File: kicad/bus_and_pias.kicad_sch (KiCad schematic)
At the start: 5 parts, among them J1 Conn_02x17_Odd_Even, U1 MC68A21, U14 74LS02, U15 74LS138, U2 MC68A21

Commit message: KiCAD: Initial PCB placement
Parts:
- J1: footprint (none) -> Connector_PinHeader_2.54mm:PinHeader_2x17_P2.54mm_Vertical
- U1, U2: footprint Package_DIP:DIP-40_W15.24mm -> Package_DIP:DIP-40_W15.24mm_LongPads
- U14: footprint (none) -> Package_DIP:DIP-14_W7.62mm_LongPads
- U15: footprint (none) -> Package_DIP:DIP-16_W7.62mm_LongPads
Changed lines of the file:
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@@
       (effects (font (size 1.27 1.27)) (justify left))
     )
-    (property "Footprint" "Package_DIP:DIP-40_W15.24mm" (id 2) (at 238.76 129.54 0)
+    (property "Footprint" "Package_DIP:DIP-40_W15.24mm_LongPads" (id 2) (at 238.76 129.54 0)
       (effects (font (size 1.27 1.27)) (justify left) hide)
     )
@@
       (effects (font (size 1.27 1.27)) (justify left))
     )
-    (property "Footprint" "Package_DIP:DIP-40_W15.24mm" (id 2) (at 163.83 129.54 0)
+    (property "Footprint" "Package_DIP:DIP-40_W15.24mm_LongPads" (id 2) (at 163.83 129.54 0)
       (effects (font (size 1.27 1.27)) (justify left) hide)
     )
@@
     (property "Reference" "J1" (id 0) (at 46.99 26.67 0))
     (property "Value" "Conn_02x17_Odd_Even" (id 1) (at 46.99 29.21 0))
-    (property "Footprint" "" (id 2) (at 45.72 53.34 0)
+    (property "Footprint" "Connector_PinHeader_2.54mm:PinHeader_2x17_P2.54mm_Vertical" (id 2) (at 45.72 53.34 0)
       (effects (font (size 1.27 1.27)) hide)
     )
@@
       (effects (font (size 1.27 1.27)) (justify left))
     )
-    (property "Footprint" "" (id 2) (at 101.6 121.92 0)
+    (property "Footprint" "Package_DIP:DIP-16_W7.62mm_LongPads" (id 2) (at 101.6 121.92 0)
       (effects (font (size 1.27 1.27)) hide)
     )
@@
     (property "Reference" "U14" (id 0) (at 85.09 57.15 0))
     (property "Value" "74LS02" (id 1) (at 85.09 59.69 0))
-    (property "Footprint" "" (id 2) (at 85.09 66.04 0)
+    (property "Footprint" "Package_DIP:DIP-14_W7.62mm_LongPads" (id 2) (at 85.09 66.04 0)
       (effects (font (size 1.27 1.27)) hide)
     )
@@
     (property "Reference" "U14" (id 0) (at 100.33 59.69 0))
     (property "Value" "74LS02" (id 1) (at 100.33 62.23 0))
-    (property "Footprint" "" (id 2) (at 100.33 68.58 0)
+    (property "Footprint" "Package_DIP:DIP-14_W7.62mm_LongPads" (id 2) (at 100.33 68.58 0)
       (effects (font (size 1.27 1.27)) hide)
     )
@@
       (effects (font (size 1.27 1.27)) (justify left))
     )
-    (property "Footprint" "" (id 2) (at 46.99 120.65 0)
+    (property "Footprint" "Package_DIP:DIP-14_W7.62mm_LongPads" (id 2) (at 46.99 120.65 0)
       (effects (font (size 1.27 1.27)) hide)
     )
@@
     (property "Reference" "U14" (id 0) (at 100.33 93.98 0))
     (property "Value" "74LS02" (id 1) (at 100.33 91.44 0))
-    (property "Footprint" "" (id 2) (at 100.33 85.09 0)
-      (effects (font (size 1.27 1.27)) hide)
-    )
+    (property "Footprint" "Package_DIP:DIP-14_W7.62mm_LongPads" (id 2) (at 100.33 85.09 0)
+      (effects (font (size 1.27 1.27)) hide)
+    )

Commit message: KiCAD: PCB now routed
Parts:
- J1: footprint Connector_PinHeader_2.54mm:PinHeader_2x17_P2.54mm_Vertical -> custom_footprints:TransitionHeader_34_P2.54mm_Vertical
- U1, U2: footprint Package_DIP:DIP-40_W15.24mm_LongPads -> Package_DIP:DIP-40_W15.24mm
- U14: footprint Package_DIP:DIP-14_W7.62mm_LongPads -> Package_DIP:DIP-14_W7.62mm
- U15: footprint Package_DIP:DIP-16_W7.62mm_LongPads -> Package_DIP:DIP-16_W7.62mm
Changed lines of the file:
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@@
       (effects (font (size 1.27 1.27)) (justify left))
     )
-    (property "Footprint" "Package_DIP:DIP-40_W15.24mm_LongPads" (id 2) (at 238.76 129.54 0)
+    (property "Footprint" "Package_DIP:DIP-40_W15.24mm" (id 2) (at 238.76 129.54 0)
       (effects (font (size 1.27 1.27)) (justify left) hide)
     )
@@
       (effects (font (size 1.27 1.27)) (justify left))
     )
-    (property "Footprint" "Package_DIP:DIP-40_W15.24mm_LongPads" (id 2) (at 163.83 129.54 0)
+    (property "Footprint" "Package_DIP:DIP-40_W15.24mm" (id 2) (at 163.83 129.54 0)
       (effects (font (size 1.27 1.27)) (justify left) hide)
     )
@@
     (property "Reference" "J1" (id 0) (at 46.99 26.67 0))
     (property "Value" "Conn_02x17_Odd_Even" (id 1) (at 46.99 29.21 0))
-    (property "Footprint" "Connector_PinHeader_2.54mm:PinHeader_2x17_P2.54mm_Vertical" (id 2) (at 45.72 53.34 0)
+    (property "Footprint" "custom_footprints:TransitionHeader_34_P2.54mm_Vertical" (id 2) (at 45.72 53.34 0)
       (effects (font (size 1.27 1.27)) hide)
     )
@@
       (effects (font (size 1.27 1.27)) (justify left))
     )
-    (property "Footprint" "Package_DIP:DIP-16_W7.62mm_LongPads" (id 2) (at 101.6 121.92 0)
+    (property "Footprint" "Package_DIP:DIP-16_W7.62mm" (id 2) (at 101.6 121.92 0)
       (effects (font (size 1.27 1.27)) hide)
     )
@@
     (property "Reference" "U14" (id 0) (at 85.09 57.15 0))
     (property "Value" "74LS02" (id 1) (at 85.09 59.69 0))
-    (property "Footprint" "Package_DIP:DIP-14_W7.62mm_LongPads" (id 2) (at 85.09 66.04 0)
+    (property "Footprint" "Package_DIP:DIP-14_W7.62mm" (id 2) (at 85.09 66.04 0)
       (effects (font (size 1.27 1.27)) hide)
     )
@@
     (property "Reference" "U14" (id 0) (at 100.33 59.69 0))
     (property "Value" "74LS02" (id 1) (at 100.33 62.23 0))
-    (property "Footprint" "Package_DIP:DIP-14_W7.62mm_LongPads" (id 2) (at 100.33 68.58 0)
+    (property "Footprint" "Package_DIP:DIP-14_W7.62mm" (id 2) (at 100.33 68.58 0)
       (effects (font (size 1.27 1.27)) hide)
     )
@@
       (effects (font (size 1.27 1.27)) (justify left))
     )
-    (property "Footprint" "Package_DIP:DIP-14_W7.62mm_LongPads" (id 2) (at 46.99 120.65 0)
+    (property "Footprint" "Package_DIP:DIP-14_W7.62mm" (id 2) (at 46.99 120.65 0)
       (effects (font (size 1.27 1.27)) hide)
     )
@@
     (property "Reference" "U14" (id 0) (at 100.33 93.98 0))
     (property "Value" "74LS02" (id 1) (at 100.33 91.44 0))
-    (property "Footprint" "Package_DIP:DIP-14_W7.62mm_LongPads" (id 2) (at 100.33 85.09 0)
-      (effects (font (size 1.27 1.27)) hide)
-    )
+    (property "Footprint" "Package_DIP:DIP-14_W7.62mm" (id 2) (at 100.33 85.09 0)
+      (effects (font (size 1.27 1.27)) hide)
+    )

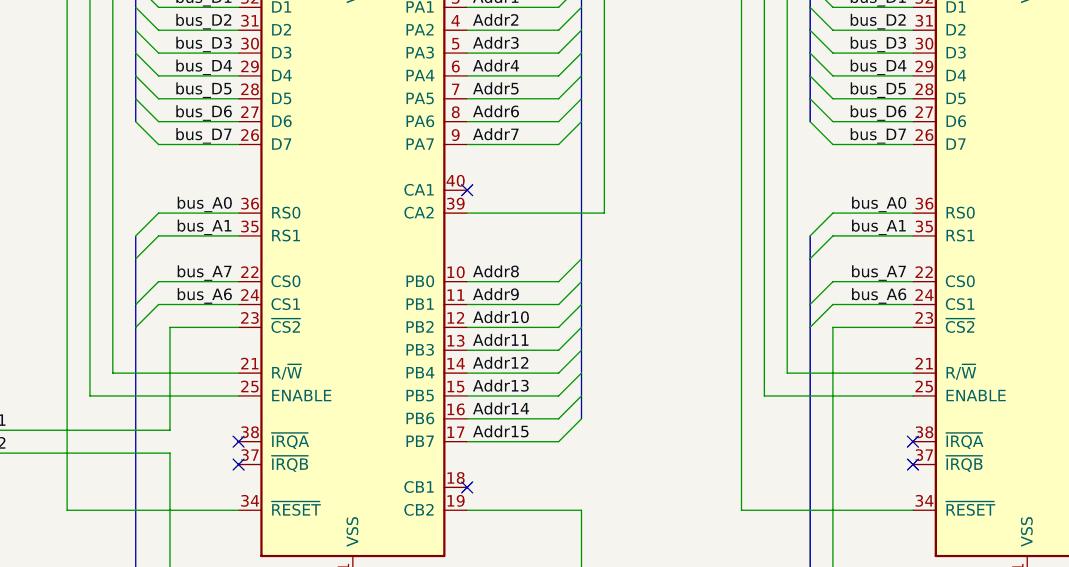
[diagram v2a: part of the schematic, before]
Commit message: KiCAD: Replace transition header with normal pin header
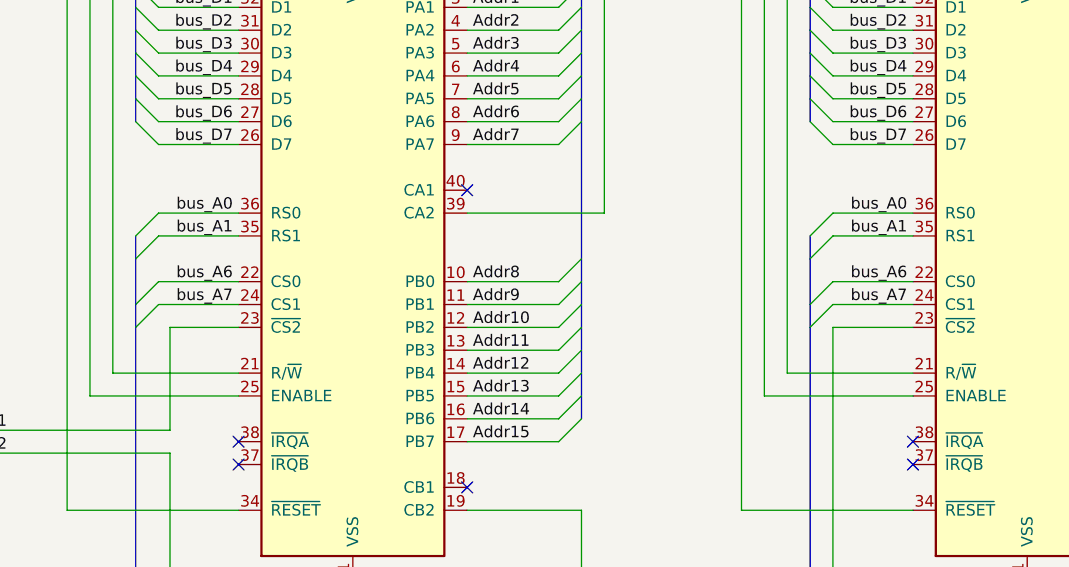
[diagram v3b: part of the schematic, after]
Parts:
- J1: footprint custom_footprints:TransitionHeader_34_P2.54mm_Vertical -> Connector_PinHeader_2.54mm:PinHeader_2x17_P2.54mm_Vertical
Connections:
- net bus_A6: now also U1.22 (CS0), U2.22 (CS0); no longer U1.24 (CS1), U2.24 (CS1)
- net bus_A7: now also U1.24 (CS1), U2.24 (CS1); no longer U1.22 (CS0), U2.22 (CS0)
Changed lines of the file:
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@@
     (effects (font (size 1.27 1.27)) (justify left bottom))
   )
-  (label "bus_A7" (at 224.155 97.79 180)
+  (label "bus_A6" (at 224.155 97.79 180)
     (effects (font (size 1.27 1.27)) (justify right bottom))
   )
@@
     (effects (font (size 1.27 1.27)) (justify left bottom))
   )
-  (label "bus_A6" (at 224.155 100.33 180)
+  (label "bus_A7" (at 224.155 100.33 180)
     (effects (font (size 1.27 1.27)) (justify right bottom))
   )
@@
     (effects (font (size 1.27 1.27)) (justify left bottom))
   )
-  (label "bus_A6" (at 149.225 100.33 180)
+  (label "bus_A7" (at 149.225 100.33 180)
     (effects (font (size 1.27 1.27)) (justify right bottom))
   )
@@
     (effects (font (size 1.27 1.27)) (justify left bottom))
   )
-  (label "bus_A7" (at 149.225 97.79 180)
+  (label "bus_A6" (at 149.225 97.79 180)
     (effects (font (size 1.27 1.27)) (justify right bottom))
   )
@@
     (property "Reference" "J1" (id 0) (at 46.99 26.67 0))
     (property "Value" "Conn_02x17_Odd_Even" (id 1) (at 46.99 29.21 0))
-    (property "Footprint" "custom_footprints:TransitionHeader_34_P2.54mm_Vertical" (id 2) (at 45.72 53.34 0)
+    (property "Footprint" "Connector_PinHeader_2.54mm:PinHeader_2x17_P2.54mm_Vertical" (id 2) (at 45.72 53.34 0)
       (effects (font (size 1.27 1.27)) hide)
     )

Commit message: KiCAD - more silk screen
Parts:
- U1, U2: footprint Package_DIP:DIP-40_W15.24mm -> Package_DIP:DIP-40_W15.24mm_Socket
- U14: footprint Package_DIP:DIP-14_W7.62mm -> Package_DIP:DIP-14_W7.62mm_Socket
- U15: footprint Package_DIP:DIP-16_W7.62mm -> Package_DIP:DIP-16_W7.62mm_Socket
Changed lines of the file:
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@@
       (effects (font (size 1.27 1.27)) (justify left))
     )
-    (property "Footprint" "Package_DIP:DIP-40_W15.24mm" (id 2) (at 238.76 129.54 0)
+    (property "Footprint" "Package_DIP:DIP-40_W15.24mm_Socket" (id 2) (at 238.76 129.54 0)
       (effects (font (size 1.27 1.27)) (justify left) hide)
     )
@@
       (effects (font (size 1.27 1.27)) (justify left))
     )
-    (property "Footprint" "Package_DIP:DIP-40_W15.24mm" (id 2) (at 163.83 129.54 0)
+    (property "Footprint" "Package_DIP:DIP-40_W15.24mm_Socket" (id 2) (at 163.83 129.54 0)
       (effects (font (size 1.27 1.27)) (justify left) hide)
     )
@@
       (effects (font (size 1.27 1.27)) (justify left))
     )
-    (property "Footprint" "Package_DIP:DIP-16_W7.62mm" (id 2) (at 101.6 121.92 0)
+    (property "Footprint" "Package_DIP:DIP-16_W7.62mm_Socket" (id 2) (at 101.6 121.92 0)
       (effects (font (size 1.27 1.27)) hide)
     )
@@
     (property "Reference" "U14" (id 0) (at 85.09 57.15 0))
     (property "Value" "74LS02" (id 1) (at 85.09 59.69 0))
-    (property "Footprint" "Package_DIP:DIP-14_W7.62mm" (id 2) (at 85.09 66.04 0)
+    (property "Footprint" "Package_DIP:DIP-14_W7.62mm_Socket" (id 2) (at 85.09 66.04 0)
       (effects (font (size 1.27 1.27)) hide)
     )
@@
     (property "Reference" "U14" (id 0) (at 100.33 59.69 0))
     (property "Value" "74LS02" (id 1) (at 100.33 62.23 0))
-    (property "Footprint" "Package_DIP:DIP-14_W7.62mm" (id 2) (at 100.33 68.58 0)
+    (property "Footprint" "Package_DIP:DIP-14_W7.62mm_Socket" (id 2) (at 100.33 68.58 0)
       (effects (font (size 1.27 1.27)) hide)
     )
@@
       (effects (font (size 1.27 1.27)) (justify left))
     )
-    (property "Footprint" "Package_DIP:DIP-14_W7.62mm" (id 2) (at 46.99 120.65 0)
+    (property "Footprint" "Package_DIP:DIP-14_W7.62mm_Socket" (id 2) (at 46.99 120.65 0)
       (effects (font (size 1.27 1.27)) hide)
     )
@@
     (property "Reference" "U14" (id 0) (at 100.33 93.98 0))
     (property "Value" "74LS02" (id 1) (at 100.33 91.44 0))
-    (property "Footprint" "Package_DIP:DIP-14_W7.62mm" (id 2) (at 100.33 85.09 0)
-      (effects (font (size 1.27 1.27)) hide)
-    )
+    (property "Footprint" "Package_DIP:DIP-14_W7.62mm_Socket" (id 2) (at 100.33 85.09 0)
+      (effects (font (size 1.27 1.27)) hide)
+    )

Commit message: KiCAD: Customize IC footprint silk screen
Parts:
- U1, U2: footprint Package_DIP:DIP-40_W15.24mm_Socket -> custom_footprints:DIP-40_W15.24mm_Socket
- U14: footprint Package_DIP:DIP-14_W7.62mm_Socket -> custom_footprints:DIP-14_W7.62mm_Socket
- U15: footprint Package_DIP:DIP-16_W7.62mm_Socket -> custom_footprints:DIP-16_W7.62mm_Socket
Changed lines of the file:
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@@
       (effects (font (size 1.27 1.27)) (justify left))
     )
-    (property "Footprint" "Package_DIP:DIP-40_W15.24mm_Socket" (id 2) (at 238.76 129.54 0)
+    (property "Footprint" "custom_footprints:DIP-40_W15.24mm_Socket" (id 2) (at 238.76 129.54 0)
       (effects (font (size 1.27 1.27)) (justify left) hide)
     )
@@
       (effects (font (size 1.27 1.27)) (justify left))
     )
-    (property "Footprint" "Package_DIP:DIP-40_W15.24mm_Socket" (id 2) (at 163.83 129.54 0)
+    (property "Footprint" "custom_footprints:DIP-40_W15.24mm_Socket" (id 2) (at 163.83 129.54 0)
       (effects (font (size 1.27 1.27)) (justify left) hide)
     )
@@
       (effects (font (size 1.27 1.27)) (justify left))
     )
-    (property "Footprint" "Package_DIP:DIP-16_W7.62mm_Socket" (id 2) (at 101.6 121.92 0)
+    (property "Footprint" "custom_footprints:DIP-16_W7.62mm_Socket" (id 2) (at 101.6 121.92 0)
       (effects (font (size 1.27 1.27)) hide)
     )
@@
     (property "Reference" "U14" (id 0) (at 85.09 57.15 0))
     (property "Value" "74LS02" (id 1) (at 85.09 59.69 0))
-    (property "Footprint" "Package_DIP:DIP-14_W7.62mm_Socket" (id 2) (at 85.09 66.04 0)
+    (property "Footprint" "custom_footprints:DIP-14_W7.62mm_Socket" (id 2) (at 85.09 66.04 0)
       (effects (font (size 1.27 1.27)) hide)
     )
@@
     (property "Reference" "U14" (id 0) (at 100.33 59.69 0))
     (property "Value" "74LS02" (id 1) (at 100.33 62.23 0))
-    (property "Footprint" "Package_DIP:DIP-14_W7.62mm_Socket" (id 2) (at 100.33 68.58 0)
+    (property "Footprint" "custom_footprints:DIP-14_W7.62mm_Socket" (id 2) (at 100.33 68.58 0)
       (effects (font (size 1.27 1.27)) hide)
     )
@@
       (effects (font (size 1.27 1.27)) (justify left))
     )
-    (property "Footprint" "Package_DIP:DIP-14_W7.62mm_Socket" (id 2) (at 46.99 120.65 0)
+    (property "Footprint" "custom_footprints:DIP-14_W7.62mm_Socket" (id 2) (at 46.99 120.65 0)
       (effects (font (size 1.27 1.27)) hide)
     )
@@
     (property "Reference" "U14" (id 0) (at 100.33 93.98 0))
     (property "Value" "74LS02" (id 1) (at 100.33 91.44 0))
-    (property "Footprint" "Package_DIP:DIP-14_W7.62mm_Socket" (id 2) (at 100.33 85.09 0)
-      (effects (font (size 1.27 1.27)) hide)
-    )
+    (property "Footprint" "custom_footprints:DIP-14_W7.62mm_Socket" (id 2) (at 100.33 85.09 0)
+      (effects (font (size 1.27 1.27)) hide)
+    )

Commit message: KiCAD: Allow space for box header for 1MHz bus
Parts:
- J1: footprint Connector_PinHeader_2.54mm:PinHeader_2x17_P2.54mm_Vertical -> Connector_IDC:IDC-Header_2x17_P2.54mm_Vertical
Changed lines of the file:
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@@
     (property "Reference" "J1" (id 0) (at 46.99 26.67 0))
     (property "Value" "Conn_02x17_Odd_Even" (id 1) (at 46.99 29.21 0))
-    (property "Footprint" "Connector_PinHeader_2.54mm:PinHeader_2x17_P2.54mm_Vertical" (id 2) (at 45.72 53.34 0)
+    (property "Footprint" "Connector_IDC:IDC-Header_2x17_P2.54mm_Vertical" (id 2) (at 45.72 53.34 0)
       (effects (font (size 1.27 1.27)) hide)
     )
